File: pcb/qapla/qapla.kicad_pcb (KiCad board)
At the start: 2 copper layers, 163.1 x 137.1 mm, 58 parts

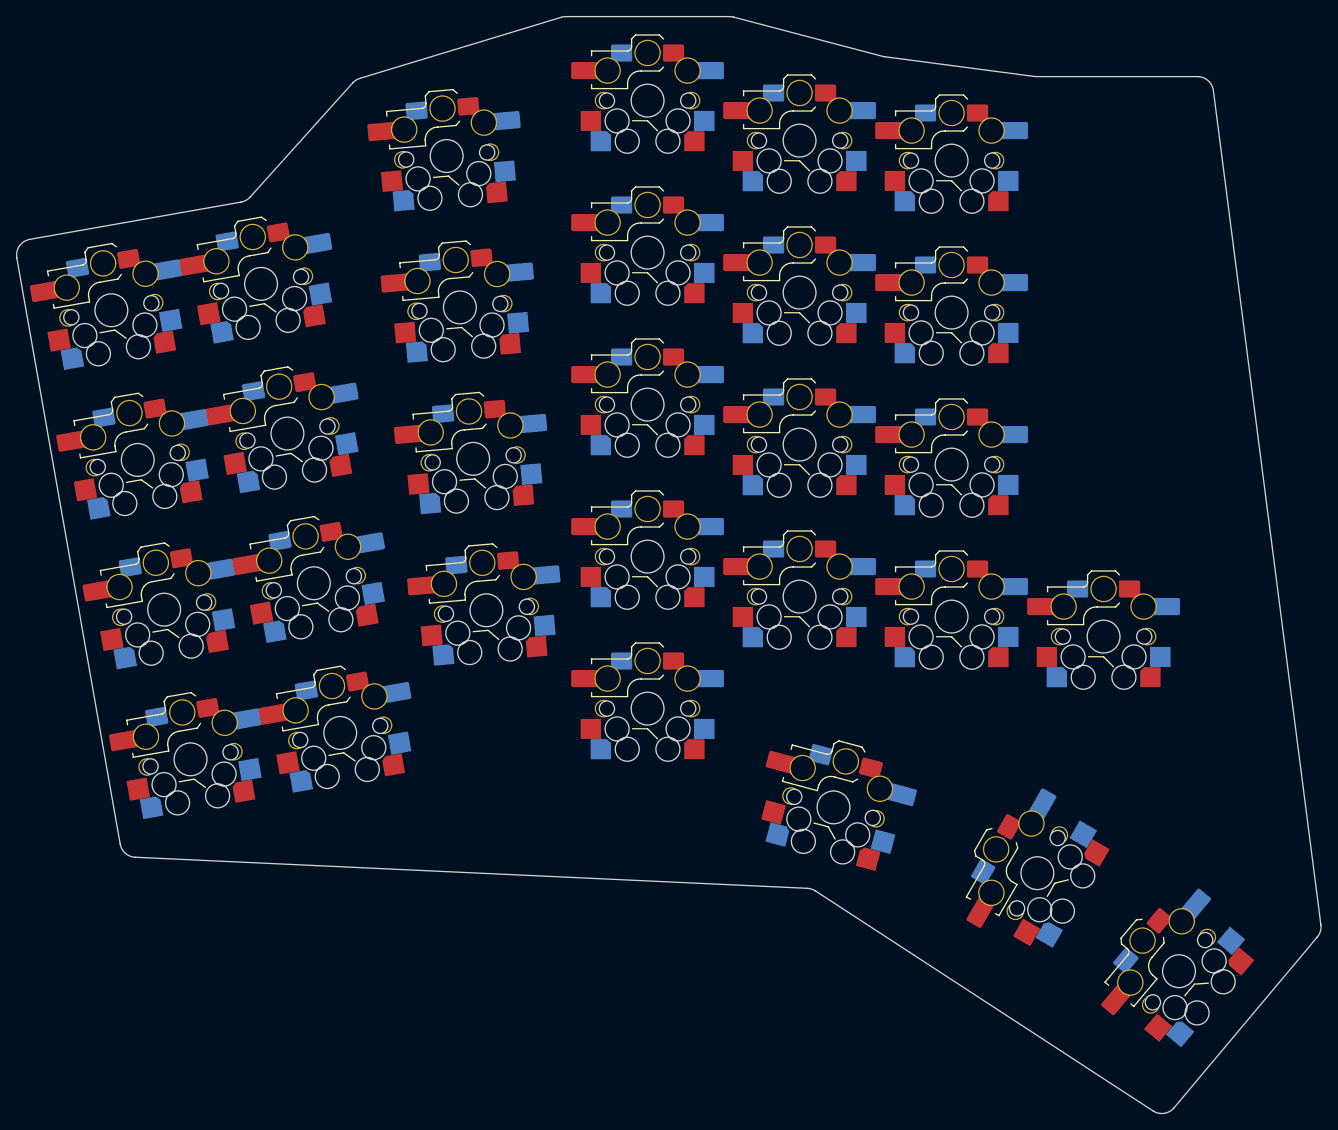
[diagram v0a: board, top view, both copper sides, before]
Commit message: Adding diodes and mcu
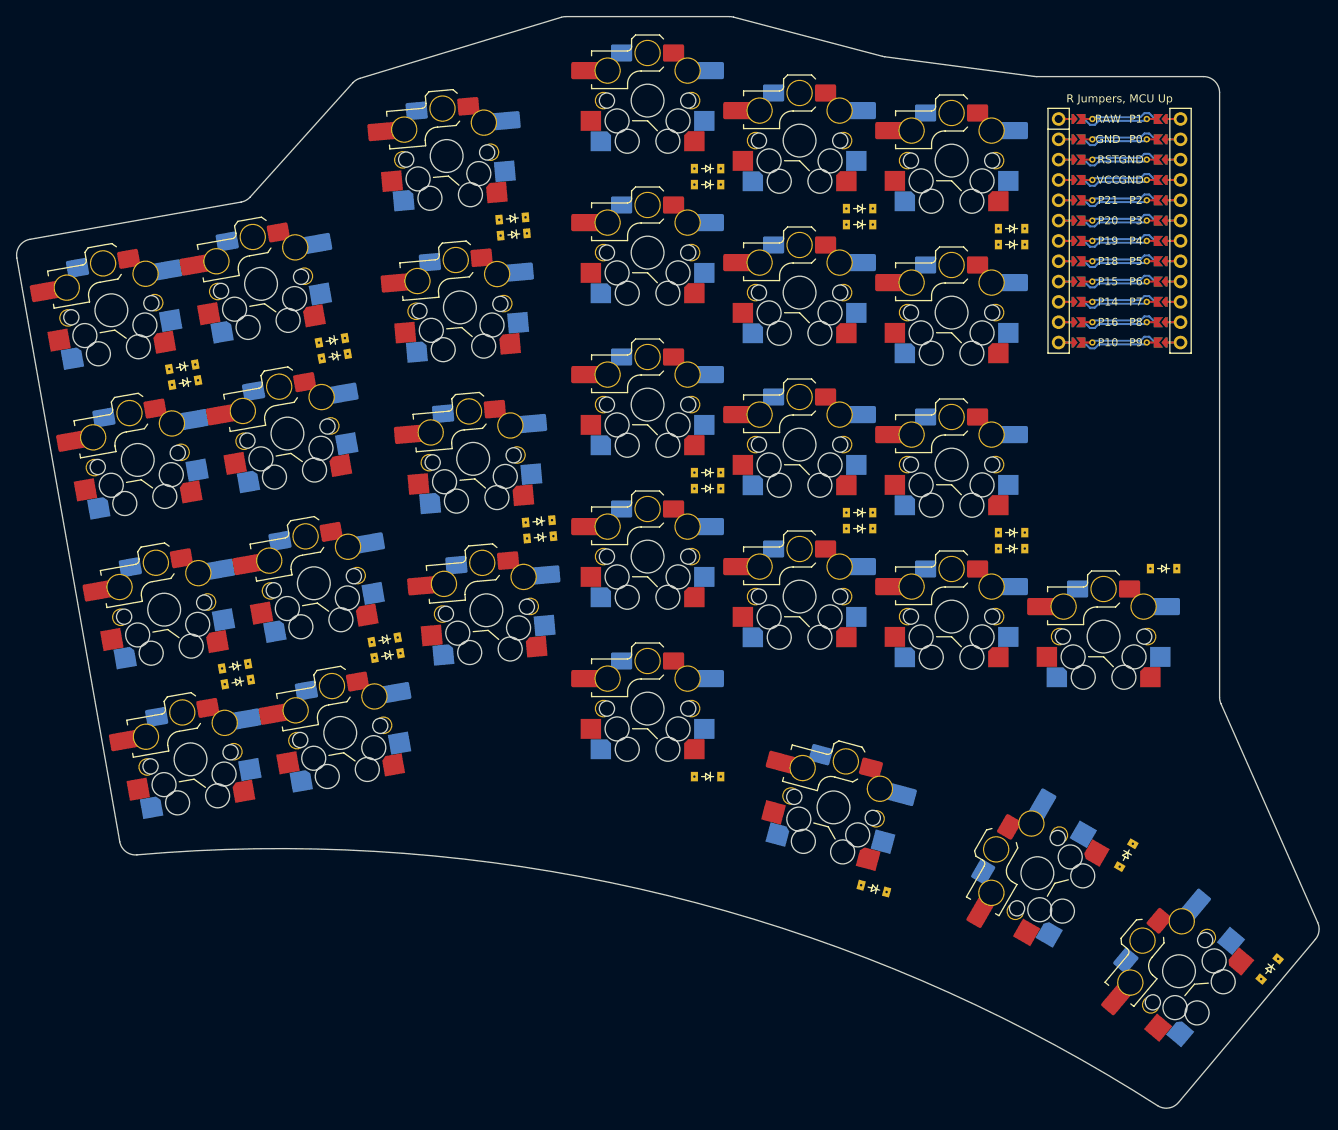
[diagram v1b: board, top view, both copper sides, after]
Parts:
- added D1: , ceoloide:diode_tht_sod123, B.Cu at (126.8, 100.0)
- added D10: , ceoloide:diode_tht_sod123, B.Cu at (204.9, 80.8)
- added D11: , ceoloide:diode_tht_sod123, B.Cu at (204.9, 42.8)
- added D12: , ceoloide:diode_tht_sod123, B.Cu at (223.9, 83.3)
- added D13: , ceoloide:diode_tht_sod123, B.Cu at (223.9, 45.3)
- added D14: , ceoloide:diode_tht_sod123, B.Cu at (206.6, 127.8)
- added D15: , ceoloide:diode_tht_sod123, B.Cu at (238.2, 123.6)
- added D16: , ceoloide:diode_tht_sod123, B.Cu at (256.1, 137.8)
- added D17: , ceoloide:diode_tht_sod123, B.Cu at (127.1, 102.0)
- added D18: , ceoloide:diode_tht_sod123, B.Cu at (120.5, 64.5)
- added D19: , ceoloide:diode_tht_sod123, B.Cu at (145.9, 98.7)
- added D2: , ceoloide:diode_tht_sod123, B.Cu at (120.2, 62.6)
- added D20: , ceoloide:diode_tht_sod123, B.Cu at (139.3, 61.2)
- added D21: , ceoloide:diode_tht_sod123, B.Cu at (164.9, 83.9)
- added D22: , ceoloide:diode_tht_sod123, B.Cu at (161.6, 46.0)
- added D23: , ceoloide:diode_tht_sod123, B.Cu at (185.9, 77.8)
- added D24: , ceoloide:diode_tht_sod123, B.Cu at (185.9, 39.8)
- added D25: , ceoloide:diode_tht_sod123, B.Cu at (204.9, 82.8)
- added D26: , ceoloide:diode_tht_sod123, B.Cu at (204.9, 44.8)
- added D27: , ceoloide:diode_tht_sod123, B.Cu at (223.9, 85.3)
- added D28: , ceoloide:diode_tht_sod123, B.Cu at (223.9, 47.3)
- added D29: , ceoloide:diode_tht_sod123, B.Cu at (242.9, 87.8)
- added D3: , ceoloide:diode_tht_sod123, B.Cu at (145.5, 96.7)
- added D4: , ceoloide:diode_tht_sod123, B.Cu at (138.9, 59.3)
- added D5: , ceoloide:diode_tht_sod123, B.Cu at (164.8, 81.9)
- added D6: , ceoloide:diode_tht_sod123, B.Cu at (161.5, 44.0)
- added D7: , ceoloide:diode_tht_sod123, B.Cu at (185.9, 113.8)
- added D8: , ceoloide:diode_tht_sod123, B.Cu at (185.9, 75.8)
- added D9: , ceoloide:diode_tht_sod123, B.Cu at (185.9, 37.8)
- added MCU1: , ceoloide:mcu_nice_nano, F.Cu at (237.4, 44.3)
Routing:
- net (no net): track 0.00 -> 337.7 mm
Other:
- board size 163.1 x 137.1 mm -> 162.8 x 136.4 mm

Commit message: Adding nets for keys, reset switch and display
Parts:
- added DISP1: , ceoloide:display_nice_view, F.Cu at (237.4, 47.8)
- added _1: , trrs_jumper, F.Cu at (247.9, 36.8)
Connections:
- D1 pad 1: (no net) -> P7
- D10 pad 1: (no net) -> P7
- D11 pad 1: (no net) -> P9
- D12 pad 1: (no net) -> P7
- D13 pad 1: (no net) -> P9
- D14 pad 1: (no net) -> P9
- D15 pad 1: (no net) -> P9
- D16 pad 1: (no net) -> P9
- D17 pad 1: (no net) -> P6
- D18 pad 1: (no net) -> P8
- D19 pad 1: (no net) -> P6
- D2 pad 1: (no net) -> P9
- D20 pad 1: (no net) -> P8
- D21 pad 1: (no net) -> P6
- D22 pad 1: (no net) -> P8
- D23 pad 1: (no net) -> P6
- D24 pad 1: (no net) -> P8
- D25 pad 1: (no net) -> P6
- D26 pad 1: (no net) -> P8
- D27 pad 1: (no net) -> P6
- D28 pad 1: (no net) -> P8
- D29 pad 1: (no net) -> P6
- D3 pad 1: (no net) -> P7
- D4 pad 1: (no net) -> P9
- D5 pad 1: (no net) -> P7
- D6 pad 1: (no net) -> P9
- D7 pad 1: (no net) -> P5
- D8 pad 1: (no net) -> P7
- D9 pad 1: (no net) -> P9
- S1 pad 1: (no net) -> P10
- S10 pad 1: (no net) -> P14
- S11 pad 1: (no net) -> P14
- S12 pad 1: (no net) -> P14
- S13 pad 1: (no net) -> P15
- S14 pad 1: (no net) -> P15
- S15 pad 1: (no net) -> P15
- S16 pad 1: (no net) -> P15
- S17 pad 1: (no net) -> P15
- S18 pad 1: (no net) -> P18
- S19 pad 1: (no net) -> P18
- S2 pad 1: (no net) -> P10
- S20 pad 1: (no net) -> P18
- S21 pad 1: (no net) -> P18
- S22 pad 1: (no net) -> P19
- S23 pad 1: (no net) -> P19
- S24 pad 1: (no net) -> P19
- S25 pad 1: (no net) -> P19
- S26 pad 1: (no net) -> P20
- S27 pad 1: (no net) -> P18
- S28 pad 1: (no net) -> P19
- S29 pad 1: (no net) -> P20
- S3 pad 1: (no net) -> P10
- S30 pad 1: (no net) -> P10
- S31 pad 1: (no net) -> P10
- S32 pad 1: (no net) -> P10
- S33 pad 1: (no net) -> P10
- S34 pad 1: (no net) -> P16
- S35 pad 1: (no net) -> P16
- S36 pad 1: (no net) -> P16
- S37 pad 1: (no net) -> P16
- S38 pad 1: (no net) -> P14
- S39 pad 1: (no net) -> P14
- S4 pad 1: (no net) -> P10
- S40 pad 1: (no net) -> P14
- S41 pad 1: (no net) -> P14
- S42 pad 1: (no net) -> P15
- S43 pad 1: (no net) -> P15
- S44 pad 1: (no net) -> P15
- S45 pad 1: (no net) -> P15
- S46 pad 1: (no net) -> P15
- S47 pad 1: (no net) -> P18
- S48 pad 1: (no net) -> P18
- S49 pad 1: (no net) -> P18
- S5 pad 1: (no net) -> P16
- S50 pad 1: (no net) -> P18
- S51 pad 1: (no net) -> P19
- S52 pad 1: (no net) -> P19
- S53 pad 1: (no net) -> P19
- S54 pad 1: (no net) -> P19
- S55 pad 1: (no net) -> P20
- S56 pad 1: (no net) -> P18
- S57 pad 1: (no net) -> P19
- S58 pad 1: (no net) -> P20
- S6 pad 1: (no net) -> P16
- S7 pad 1: (no net) -> P16
- S8 pad 1: (no net) -> P16
- S9 pad 1: (no net) -> P14

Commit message: Adding JS102011SAQN switch
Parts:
- added _2: , switch_JS102011SAQN, F.Cu at (203.9, 21.8)
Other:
- outline, holes or cut-outs redrawn

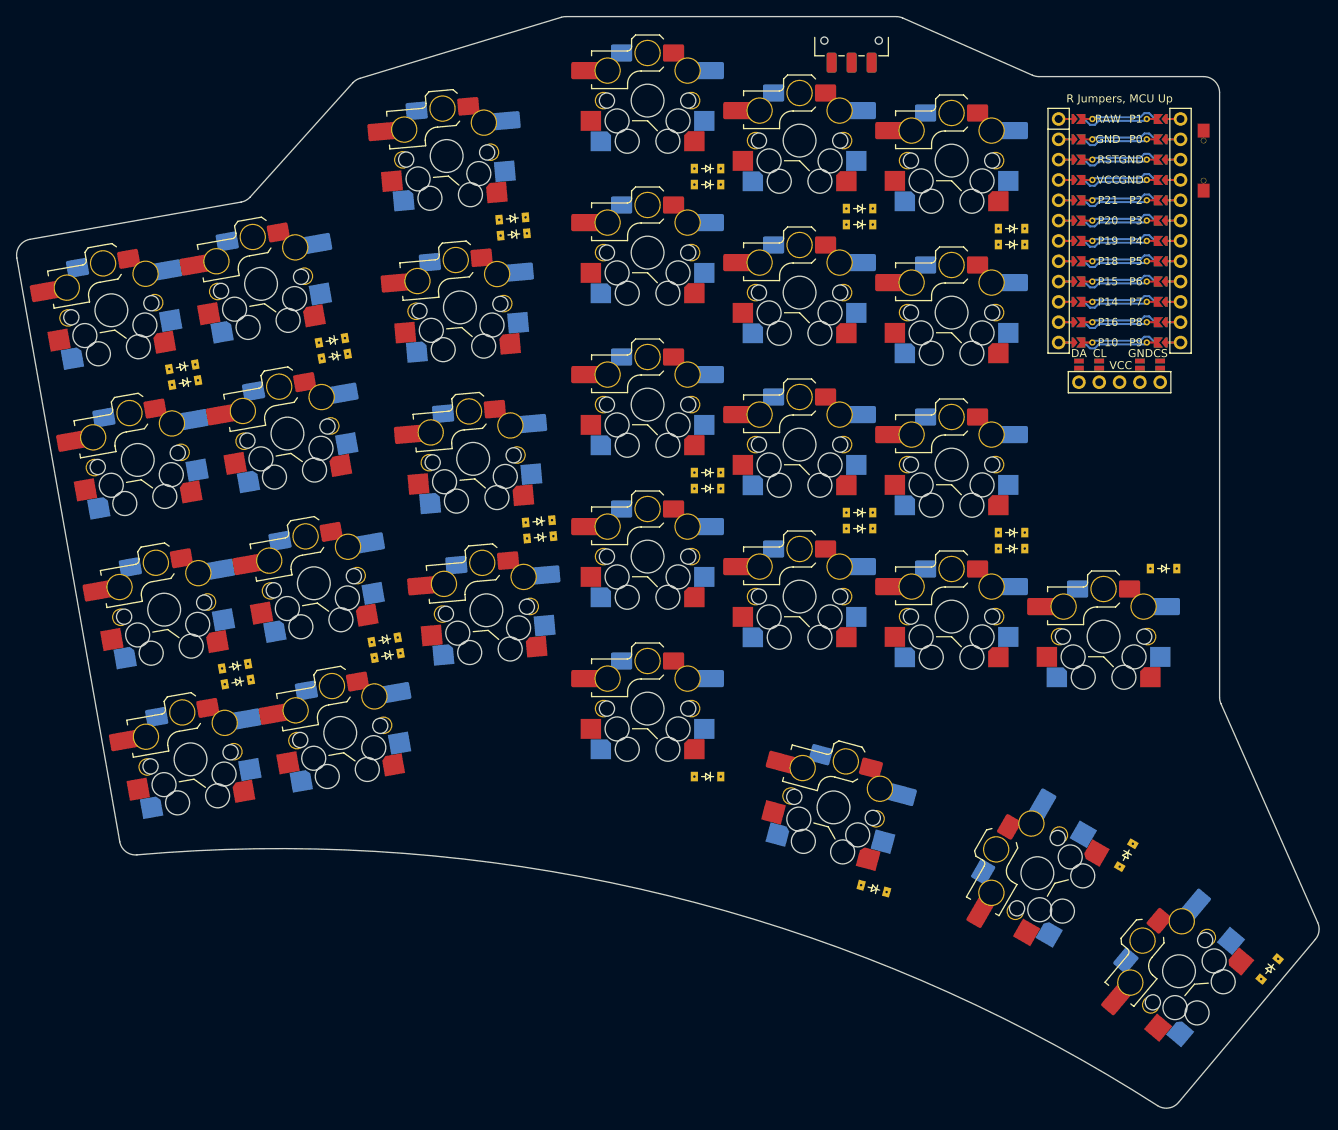
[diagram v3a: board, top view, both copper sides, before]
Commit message: Positioning reset switch, jst connector and power switch
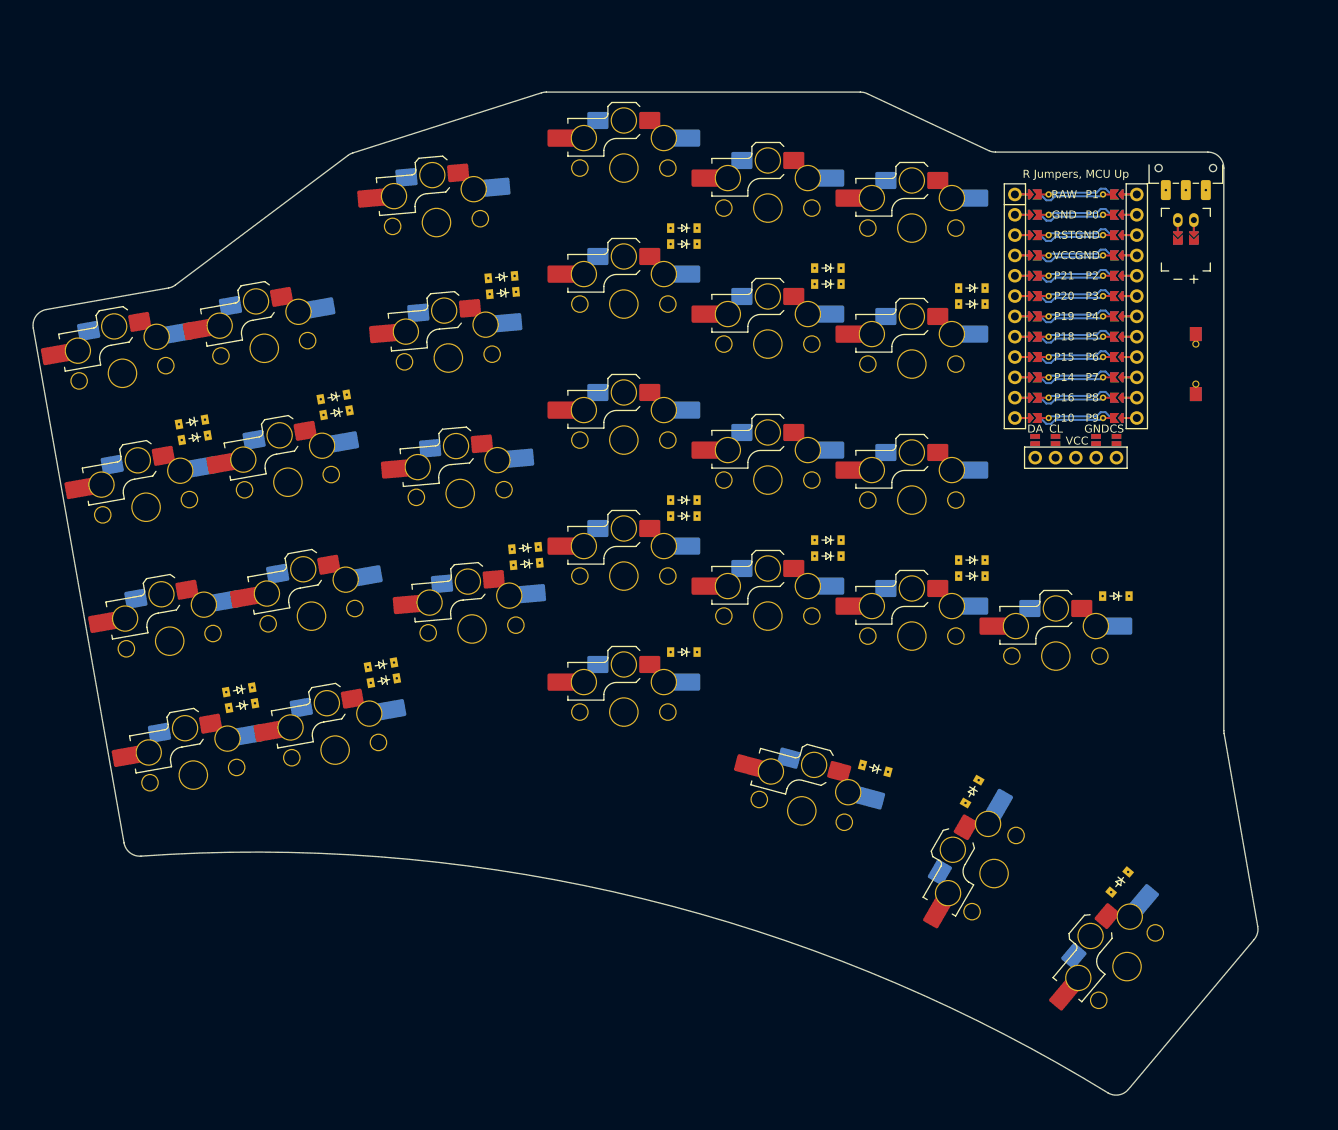
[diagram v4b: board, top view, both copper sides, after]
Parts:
- removed S30, S31, S32, S33, S34, S35, S36, S37, S38, S39, S40, S41, S42, S43, S44, S45, S46, S47, S48, S49, S50, S51, S52, S53, S54, S55, S56, S57, S58: , ceoloide:switch_mx
- added JST1: , ceoloide:battery_connector_jst_ph_2, F.Cu at (245.6, 44.2)
- moved D16 135.8 mm to (139.5, 68.3), turned to 190 degrees
- moved D13 113.2 mm to (127.7, 104.9), turned to 190 degrees
- moved D14 101.9 mm to (121.8, 71.4), turned to 190 degrees
- moved D15 95.3 mm to (145.4, 101.8), turned to 190 degrees
- moved D28 68.6 mm to (218.9, 115.7), turned to 240 degrees
- moved D24 59.0 mm to (218.9, 88.7)
- moved D26 56.4 mm to (236.9, 91.2)
- moved D22 56.2 mm to (200.9, 86.2), turned to 180 degrees
- moved D9 48.8 mm to (200.9, 84.2)
- moved D20 48.0 mm to (182.9, 81.2), turned to 180 degrees
- moved D11 46.1 mm to (218.9, 86.7)
- moved _2 44.7 mm to (245.6, 37.7)
- moved D18 41.3 mm to (160.3, 53.4), turned to 185 degrees
- moved D21 40.8 mm to (182.9, 47.2), turned to 180 degrees
- moved D29 39.6 mm to (237.4, 127.0), turned to 230 degrees
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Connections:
- D10 pad 1: P7 -> P9
- D10 pad 2: index_home -> index_num
- D11 pad 1: P9 -> P7
- D11 pad 2: index_num -> inner_home
- D12 pad 1: P7 -> P9
- D12 pad 2: inner_home -> inner_num
- D13 pad 1: P9 -> P6
- D13 pad 2: inner_num -> outer_bottom
- D14 pad 1: P9 -> P8
- D14 pad 2: alt_mod -> outer_top
- D15 pad 1: P9 -> P6
- D15 pad 2: inner_mod -> pinky_bottom
- D16 pad 1: P9 -> P8
- D16 pad 2: outer_mod -> pinky_top
- D17 pad 2: outer_bottom -> ring_bottom
- D18 pad 2: outer_top -> ring_top
- D19 pad 1: P6 -> P5
- D19 pad 2: pinky_bottom -> middle_mod
- D20 pad 1: P8 -> P6
- D20 pad 2: pinky_top -> middle_bottom
- D21 pad 1: P6 -> P8
- D21 pad 2: ring_bottom -> middle_top
- D22 pad 1: P8 -> P6
- D22 pad 2: ring_top -> index_bottom
- D23 pad 1: P6 -> P8
- D23 pad 2: middle_bottom -> index_top
- D24 pad 1: P8 -> P6
- D24 pad 2: middle_top -> inner_bottom
- D25 pad 1: P6 -> P8
- D25 pad 2: index_bottom -> inner_top
- D26 pad 1: P8 -> P6
- D26 pad 2: index_top -> inner_far_bottom
- D27 pad 1: P6 -> P9
- D27 pad 2: inner_bottom -> alt_mod
- D28 pad 1: P8 -> P9
- D28 pad 2: inner_top -> inner_mod
- D29 pad 1: P6 -> P9
- D29 pad 2: inner_far_bottom -> outer_mod
- D7 pad 1: P5 -> P7
- D7 pad 2: middle_mod -> middle_home
- D8 pad 1: P7 -> P9
- D8 pad 2: middle_home -> middle_num
- D9 pad 1: P9 -> P7
- D9 pad 2: middle_num -> index_home
- _2 pad 1: RAW -> (no net)
- _2 pad 3: (no net) -> RAW
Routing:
- net JST1_2: track 0.00 -> 3.60 mm
- net JST1_1: track 0.00 -> 3.60 mm
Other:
- board size 162.8 x 136.4 mm -> 153.1 x 125.4 mm
